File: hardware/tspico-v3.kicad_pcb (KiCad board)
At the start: 4 copper layers, 130 x 56 mm, 147 parts, among them J1 USB-C, J2 microSD, J3 OLED 1.27in 128x96, J4 3.5mm stereo, J5 Joystick, P1 TS2068_Edge, SW1 TS Reset, SW2 NMI, SW3 RUN, SW4 BOOTSEL, U1 74LVC245APW, U15 XL9555, U2 74LVC245APW, U20 RP2350B, U21 GD25Q128ESIGR, U22 APS6404L-3SQR-SN, U3 74LVC245APW, U30 TLV1117LV33, U31 TLV1117LV33, U4 74LVC245APW, U40 ESP32-C3-WROOM-02-N4, U50 MCP6002, U6 74LVC32APW, U7 74LVC06AD, Y1 12MHz

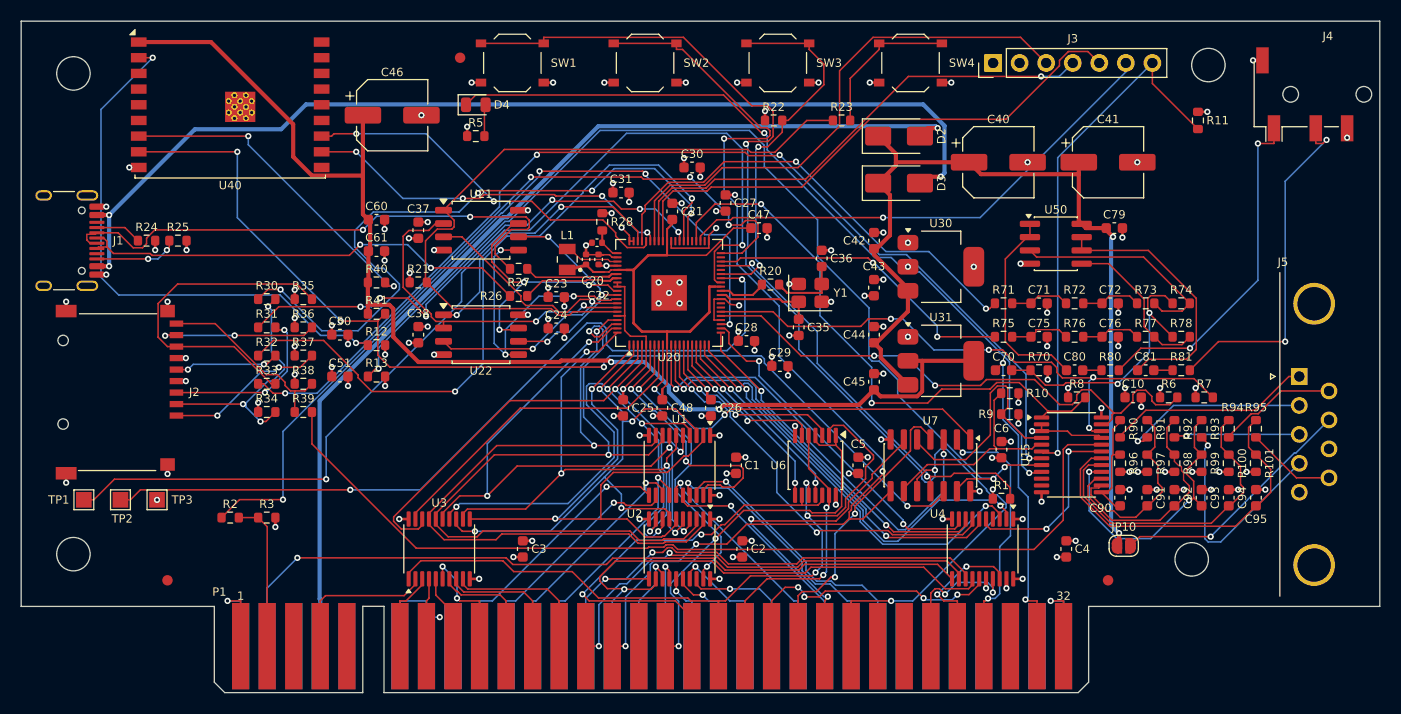
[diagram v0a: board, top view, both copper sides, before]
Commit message: flow.py: one-command flow that re-routes when the finisher cannot close the board
Freerouting is not repeatable; about one run in three leaves a U1 address pin
sealed in. finish.py now tries lifting the neighbours (rejecting via-heavy
detours), exits non-zero when the board is not clean, and flow.py routes again
from the placement. Board regenerated by flow.py: closed on attempt 2, DRC clean
at every severity, 139/140 designators on silk.

Co-Authored-By: Claude Fable 5.1 <noreply@anthropic.com>
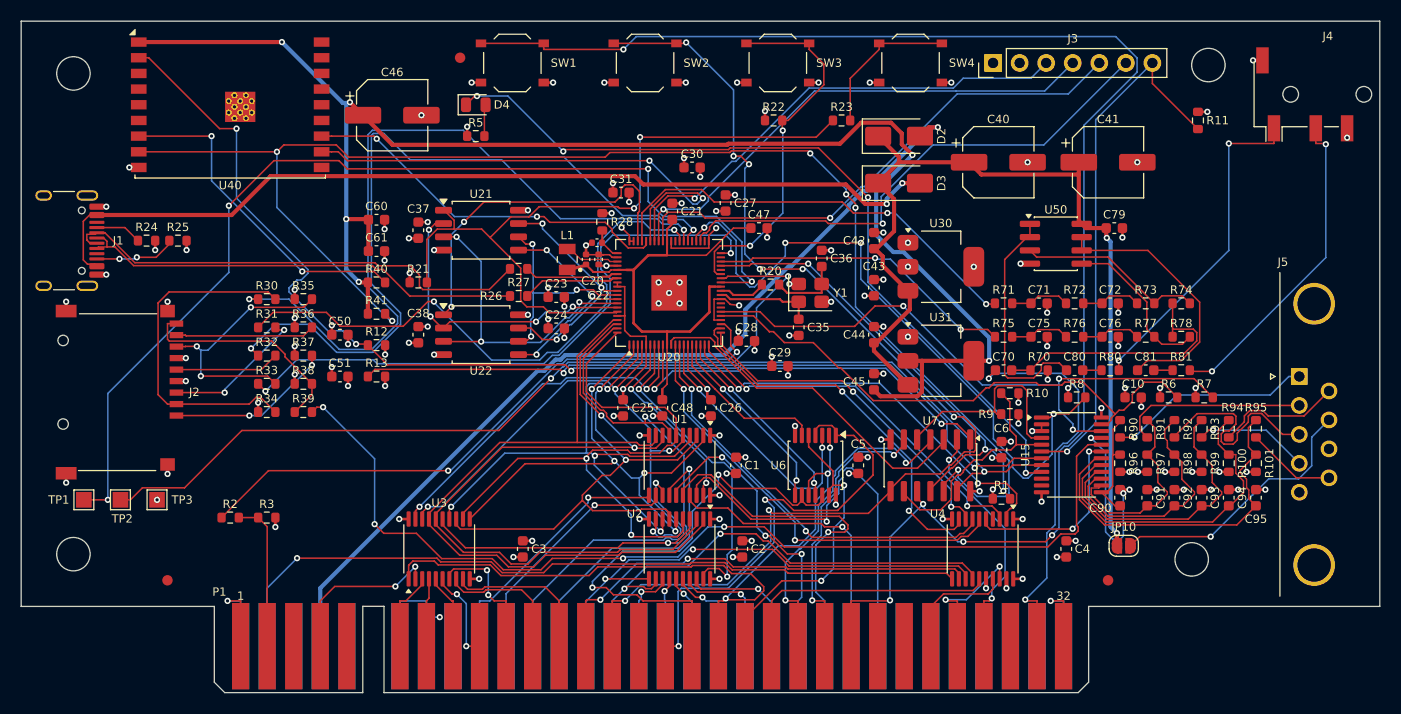
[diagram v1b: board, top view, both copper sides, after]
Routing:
- net nWIFI_BOOT: track 99.8 -> 136.7 mm, vias 4 -> 6
- net /2068 Interface/nRESET: track 115.3 -> 148.3 mm, vias 3 -> 5
- net +3V3_WIFI: track 117.6 -> 149.5 mm, vias 2 -> 6
- net WIFI_EN: track 143.3 -> 112.5 mm, vias 5 -> 4
- net WIFI_DL: track 100.8 -> 74.5 mm, vias 3 -> 2
- net TAPE_OUT: track 78.2 -> 59.4 mm, vias 4 -> 2
- net /2068 Interface/A4: track 27.7 -> 39.9 mm
- net WIFI_TX: track 35.6 -> 47.7 mm, vias 4 -> 2
- net /Joystick/JOY_RIGHT_J: track 22.3 -> 10.9 mm
- net GND: track 125.4 -> 136.6 mm, vias 102 -> 104
- net /2068 Interface/A6: track 22.5 -> 33.1 mm
- net VBUS: track 99.7 -> 89.3 mm, vias 3 -> 2
- net WAIT_REQ: track 43.6 -> 33.2 mm, vias 2 -> 0
- net MD4: track 58.6 -> 48.6 mm, vias 2 -> 4
- net /SD and Display/SD_CS_J: track 23.5 -> 33.2 mm, vias 3 -> 0
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
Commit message: Pre-route U1's address pins as a staggered via fan; flow closes first try
U1's Z80-side row faces U2 across a 0.8 mm gap, so A0-A7 can only leave under
U1's body, and the router sometimes sealed one in (A5, A3). With the fan fixed
in preroute.py three flow.py runs out of three closed on the first attempt,
DRC clean at every severity.

Co-Authored-By: Claude Fable 5.1 <noreply@anthropic.com>
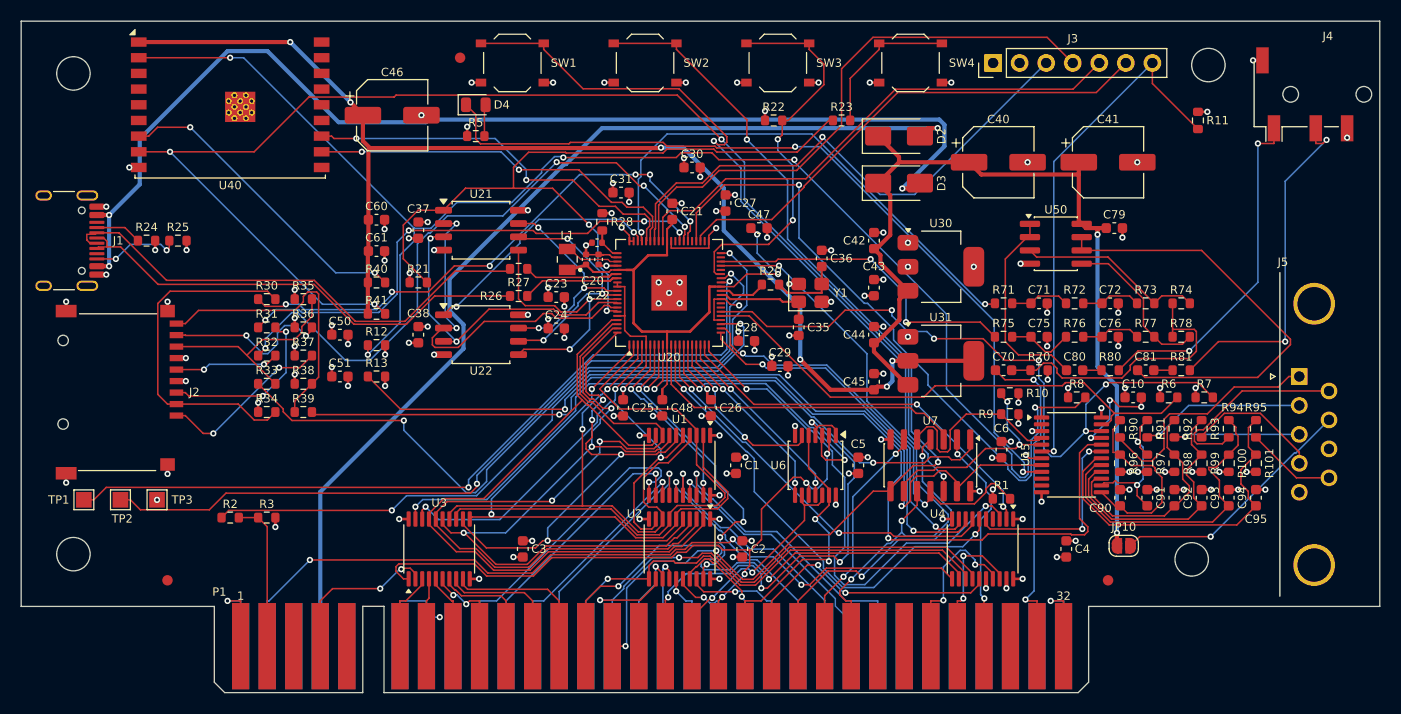
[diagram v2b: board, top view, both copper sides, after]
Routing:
- net /2068 Interface/nRESET: track 148.3 -> 99.3 mm, vias 5 -> 3
- net +3V3_WIFI: track 149.5 -> 118.7 mm
- net /2068 Interface/nIORQ: track 46.1 -> 22.6 mm
- net /RP2350B Core/SWCLK: track 98.3 -> 75.4 mm, vias 4 -> 2
- net SD_CS: track 73.9 -> 51.7 mm, vias 2 -> 6
- net VBUS: track 89.3 -> 109.0 mm, vias 2 -> 3
- net WIFI_EN: track 112.5 -> 131.7 mm, vias 4 -> 5
- net /Audio/R_OUT: track 25.5 -> 41.5 mm
- net nEXROM_L: track 36.1 -> 49.3 mm
- net SD_SCK: track 72.6 -> 60.7 mm, vias 2 -> 4
- net WIFI_TX: track 47.7 -> 36.7 mm
- net /2068 Interface/A4: track 39.9 -> 29.3 mm
- net /RP2350B Core/PSRAM_CS: track 33.5 -> 23.8 mm
- net +5V_EDGE: track 86.5 -> 96.1 mm
- net SD_MISO: track 58.9 -> 68.2 mm
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
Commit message: v3 prototype 2: bus pull-ups, SD socket power switch, PSRAM footprint
Fixes from proto1 bring-up and issue #21:

- R14 2k2 from nBE (edge A29) to +5V_EDGE. The 74LVC06 only pulls /BE
  low; without a pull-up it rose too slowly and a RAM opcode fetch after
  a served byte read wrong bits. Same value as the bodge on board 1.
- R15-R17 10k pull-ups on GP8-GP10 (nAEN_LO, nAEN_HI, nDATA_OE). The
  RP2350 resets its pads with pull-downs, so in reset and BOOTSEL all
  three buffers were enabled and U1 and U2 both drove MD.
- U32 SY6280AAC current-limited switch on the SD socket's VDD (+3V3_SD),
  enabled from XL9555 P0.6 (SD_PWR_EN), held off by R43 until the
  firmware sets it; R42 15k sets 0.45 A. A card that latches up hits the
  limit instead of pulling +3V3 down and resetting the RP2350B, and a
  wedged card can be power-cycled. R34-R37 move to +3V3_SD so they cannot
  power a switched-off card; the detect pull-up R38 stays on +3V3.
  Firmware: power on after the detect switch reads a card and before any
  SPI; release the SD pins before powering off.
- U22 footprint SOIC-8 3.9 x 4.9 mm. The APS6404L-3SQR-SN is SOP-8
  150 mil (AP Memory package code SN); proto1 had the 208 mil footprint.
  Still DNP; ESP-PSRAM64H (Adafruit 4677) fits the same pads by hand.

Routed by flow.py on the first attempt, DRC clean at every severity
(2119 segments, 385 vias). ERC: the one pre-existing U4 warning only.
$14.90/board at 10 with fees. PSRAM options surveyed in
docs/bom-cost-optimization.md.

Co-Authored-By: Claude Opus 5.5 <noreply@anthropic.com>
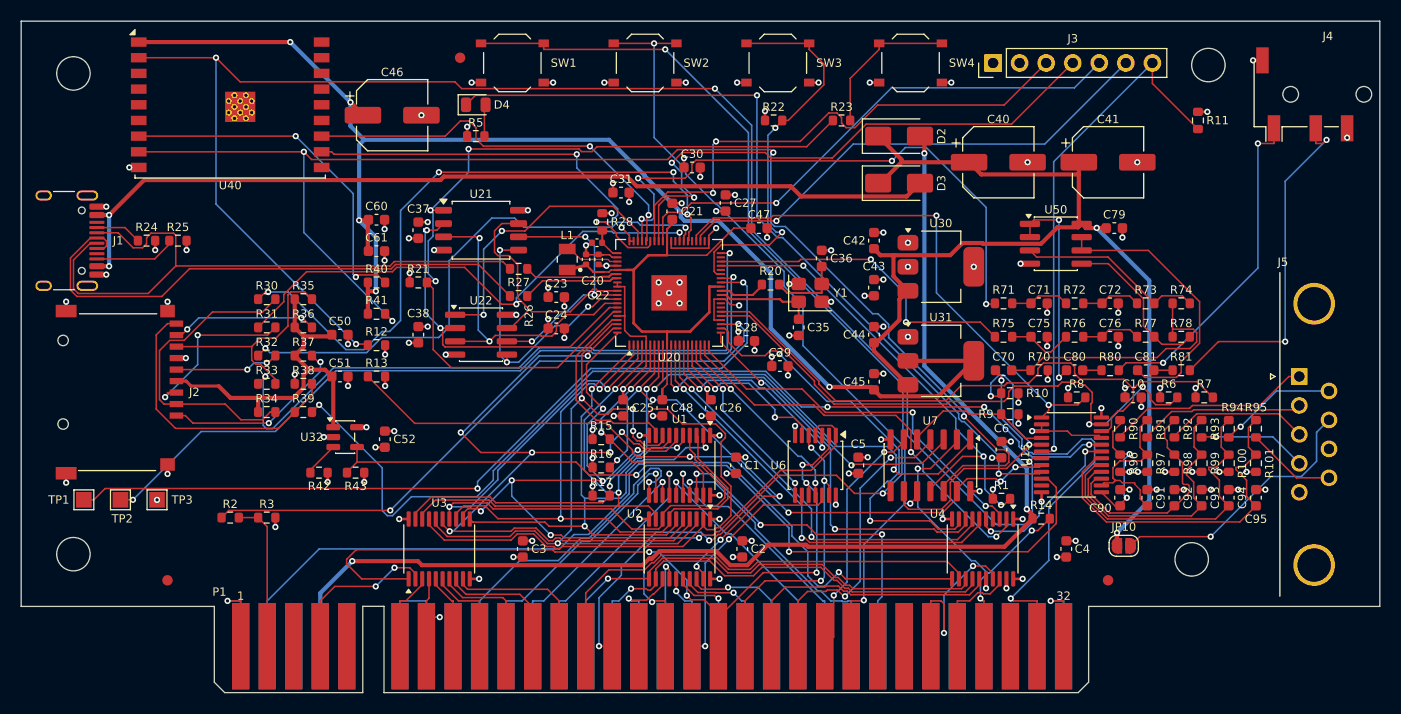
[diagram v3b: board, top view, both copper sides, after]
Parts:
- added C52: 1u, C_0603_1608Metric, F.Cu at (34.8, 40.0)
- added R14: 2k2, R_0603_1608Metric, F.Cu at (97.6, 47.6)
- added R15: 10k, R_0603_1608Metric, F.Cu at (55.5, 40.0)
- added R16: 10k, R_0603_1608Metric, F.Cu at (55.5, 42.7)
- added R17: 10k, R_0603_1608Metric, F.Cu at (55.5, 45.4)
- added R42: 15k, R_0603_1608Metric, F.Cu at (28.5, 43.2)
- added R43: 10k, R_0603_1608Metric, F.Cu at (32.0, 43.2)
- added U32: SY6280AAC, SOT-23-5, F.Cu at (31.0, 39.8)
- U22: footprint SOIC-8_5.3x5.3mm_P1.27mm -> SOIC-8_3.9x4.9mm_P1.27mm
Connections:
- C50 pad 1: +3V3 -> +3V3_SD
- C51 pad 1: +3V3 -> +3V3_SD
- J2 pad 4: +3V3 -> +3V3_SD
- R34 pad 1: +3V3 -> +3V3_SD
- R35 pad 1: +3V3 -> +3V3_SD
- R36 pad 1: +3V3 -> +3V3_SD
- R37 pad 1: +3V3 -> +3V3_SD
- U15 pad 10: unconnected-(U15-IO0_6-Pad10) -> SD_PWR_EN
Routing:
- net SD_PWR_EN: track 0.00 -> 81.7 mm, vias 0 -> 2
- net +3V3_SD: track 0.00 -> 34.7 mm
- net +5V_EDGE: track 96.1 -> 118.8 mm, vias 1 -> 3
- net WIFI_EN: track 131.7 -> 153.8 mm, vias 5 -> 4
- net VBUS: track 109.0 -> 87.7 mm, vias 3 -> 2
- net +5V: track 88.4 -> 104.4 mm
- net /Audio/R_OUT: track 41.5 -> 26.7 mm
- net nAEN_HI: track 30.0 -> 43.6 mm, vias 4 -> 6
- net /RP2350B Core/USB_DM_C: track 47.8 -> 61.2 mm
- net nIOX_INT: track 65.2 -> 52.2 mm
- net nEXROM_L: track 49.3 -> 36.6 mm
- net MD2: track 67.7 -> 80.2 mm, vias 3 -> 6
- net +3V3_WIFI: track 118.7 -> 131.1 mm, vias 6 -> 5
- net MD6: track 52.4 -> 64.4 mm
- net /2068 Interface/nBE: track 21.7 -> 33.6 mm, vias 2 -> 3
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
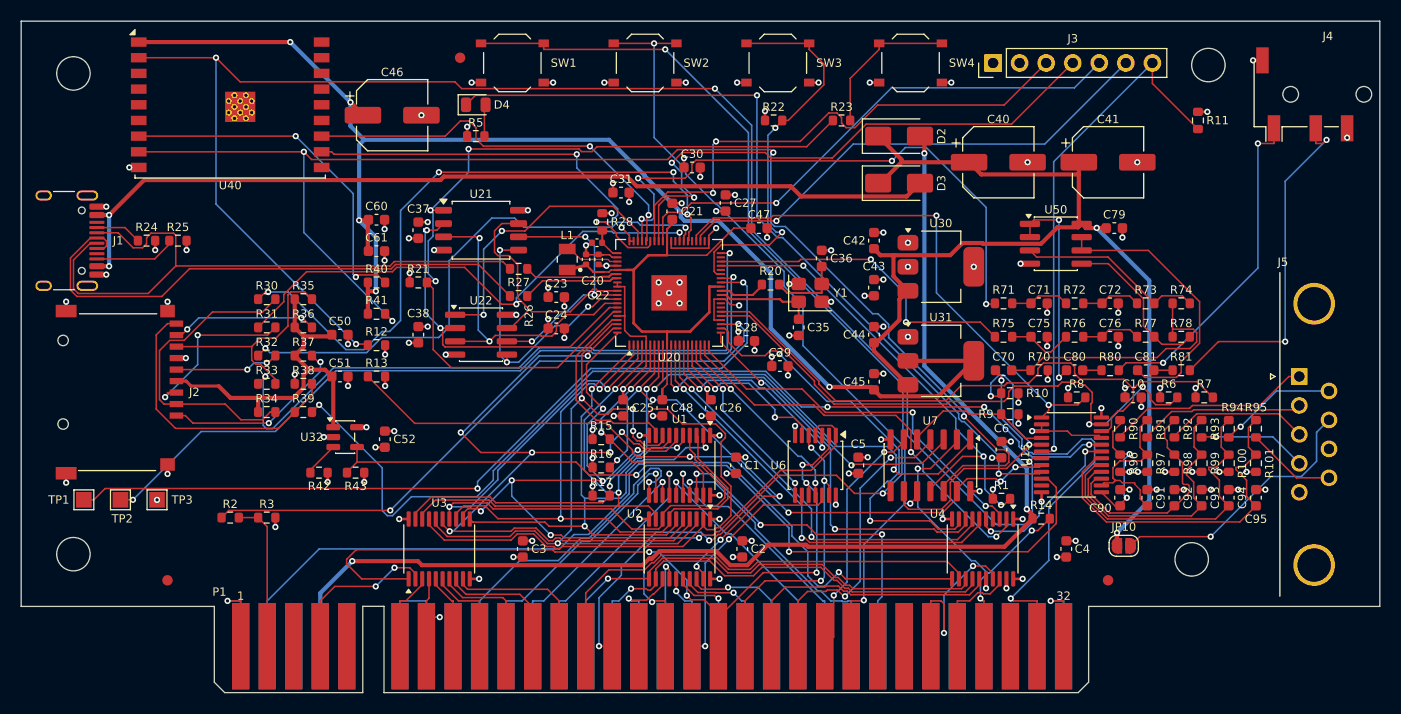
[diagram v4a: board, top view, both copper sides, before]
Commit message: v3 proto3: male DE-9, I2C OLED header, buttons in a 2x2 block
- J5: male DE-9 (CONNFLY DS1037-09MNAKT74-0CC, C75750). Atari sticks end
  in a female plug; proto1/2's female footprint mirrors every pin under a
  male part, putting the stick's ground on pin 7 (JOY_5V, open), so nothing
  read. Same body position and mounting holes as proto2.
- J3: 1x4 header for a 1.54in 128x64 SSD1309 I2C module (1 GND, 2 +3V3,
  3 SCL GP43, 4 SDA GP42) on I2C1, R44/R45 4k7 pull-ups. Replaces the 7-pin
  SSD1351 SPI header; GP34, GP41 and expander P0.2 (with R11) are freed.
- SW3 under SW1, SW4 under SW2, so the module covers no buttons; D4/R5
  move left of the ESP32, between H1 and the USB-C socket.

Routed by flow.py on the first attempt: DRC clean at every severity,
2125 segments, 373 vias. ERC: the one existing U4 warning.

Co-Authored-By: Claude Opus 5.5 <noreply@anthropic.com>
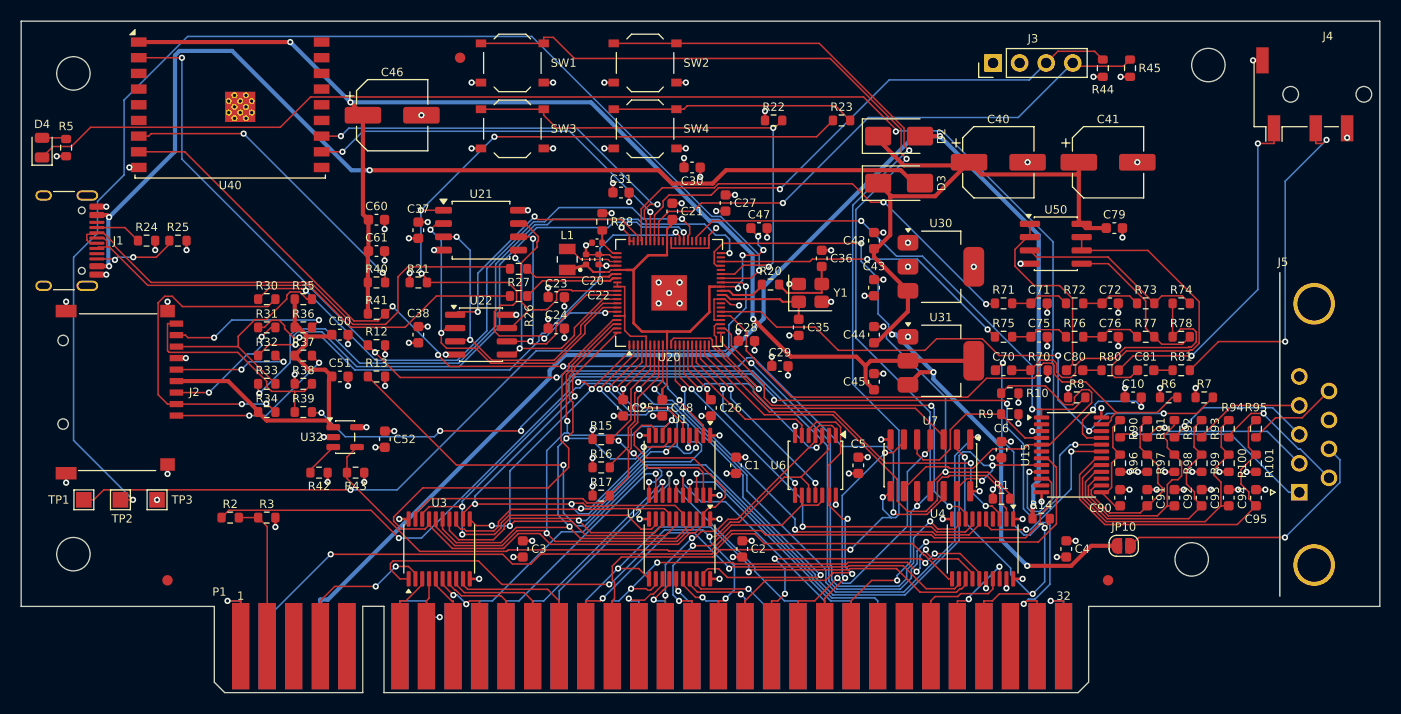
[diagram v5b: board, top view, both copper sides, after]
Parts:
- removed R11: 10k, R_0603_1608Metric
- added R44: 4k7, R_0603_1608Metric, F.Cu at (103.5, 4.50)
- added R45: 4k7, R_0603_1608Metric, F.Cu at (106.1, 4.50)
- J3: value OLED 1.27in 128x96 -> OLED 1.54in 128x64 I2C; footprint PinHeader_1x07_P2.54mm_Vertical -> PinHeader_1x04_P2.54mm_Vertical
- J5: footprint DSUB-9_Socket_Horizontal_P2.77x2.84mm_EdgePinOffset7.70mm_Housed_MountingHolesOffset9.12mm -> DSUB-9_Pins_Horizontal_P2.77x2.84mm_EdgePinOffset7.70mm_Housed_MountingHolesOffset9.12mm
- moved D4 41.7 mm to (2.00, 12.1), turned to 90 degrees
- moved R5 39.2 mm to (4.30, 12.1), turned to 90 degrees
- moved SW3 26.2 mm to (47.0, 10.3)
- moved SW4 26.2 mm to (59.7, 10.3)
- moved J5 11.1 mm to (122.3, 45.1)
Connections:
- net OLED_MOSI renamed OLED_SCL
- net OLED_SCK renamed OLED_SDA
- J3 pad 1: +3V3 -> GND
- J3 pad 2: GND -> +3V3
- U15 pad 6: nOLED_RST -> unconnected-(U15-IO0_2-Pad6)
- U20 pad 43: OLED_DC -> unconnected-(U20-GPIO34-Pad43)
- U20 pad 52: OLED_CS -> unconnected-(U20-GPIO41/ADC1-Pad52)
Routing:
- net /Local Bus and Registers/nLED: track 78.6 -> 137.5 mm
- net nOLED_RST: track 50.3 -> 0.00 mm, vias 1 -> 0
- net OLED_CS: track 50.2 -> 0.00 mm, vias 1 -> 0
- net /RP2350B Core/SWDIO: track 72.9 -> 121.2 mm
- net OLED_DC: track 48.1 -> 0.00 mm, vias 1 -> 0
- net nWIFI_BOOT: track 130.4 -> 98.0 mm
- net WIFI_DL: track 72.6 -> 96.8 mm, vias 4 -> 3
- net WIFI_EN: track 153.8 -> 134.5 mm
- net MD0: track 70.0 -> 88.6 mm
- net MD2: track 80.2 -> 61.7 mm, vias 6 -> 3
- net /2068 Interface/nRESET: track 89.6 -> 105.0 mm
- net VBUS: track 87.7 -> 103.0 mm, vias 2 -> 3
- net BE_REQ: track 41.9 -> 56.9 mm
- net /2068 Interface/nNMI: track 100.3 -> 113.0 mm, vias 4 -> 3
- net AUDIO_L: track 55.4 -> 42.8 mm, vias 4 -> 2
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
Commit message: CERN-OHL-S-2.0 licence; board labels and OSHW logo on v3 and v2.6
- LICENSE: CERN Open Hardware Licence v2, Strongly Reciprocal, for the
  hardware designs; the README says what it covers and what it does not
  (firmware/, the Pico SDK import file, Zimodem, KiCad library parts).
- hardware/scripts/labels.py: board name on the top silkscreen; name,
  repository URL (the licence's Source Location), licence and the OSHW logo
  on the bottom. Silkscreen only, rerunnable on a routed board, and it
  refuses to save a label that lands on a pad, courtyard or other silk.
  Both flow.py scripts run it last, since gen_layout.py rebuilds the board.
- Applied to the v3 and v2.6 boards: copper untouched, DRC clean at every
  severity. v3 PCB PDF and both boards' renders regenerated.

Not tagged: the labels go into each board's next revision.

Co-Authored-By: Claude Opus 5.5 <noreply@anthropic.com>
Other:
- board text added: "CERN-OHL-S-2.0"
- board text added: "TS-Pico v3"
- board text added: "github.com/factus10/tspico-hardware"
